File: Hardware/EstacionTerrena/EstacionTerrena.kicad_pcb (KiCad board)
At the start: 2 copper layers, 40 x 30 mm, 63 parts, among them J1 5-1814832-1, J2 USB_B_Micro, J3 ICSP, U1 TPD2E2U06, U2 MIC5353-3.3YMT, U3 PIC18F14K50, U4 CC1101RGP, U5 0915BM15A0001E, U6 B39921B3588U410, U7 CC1190, Y1 12MHz, Y2 26 MHz

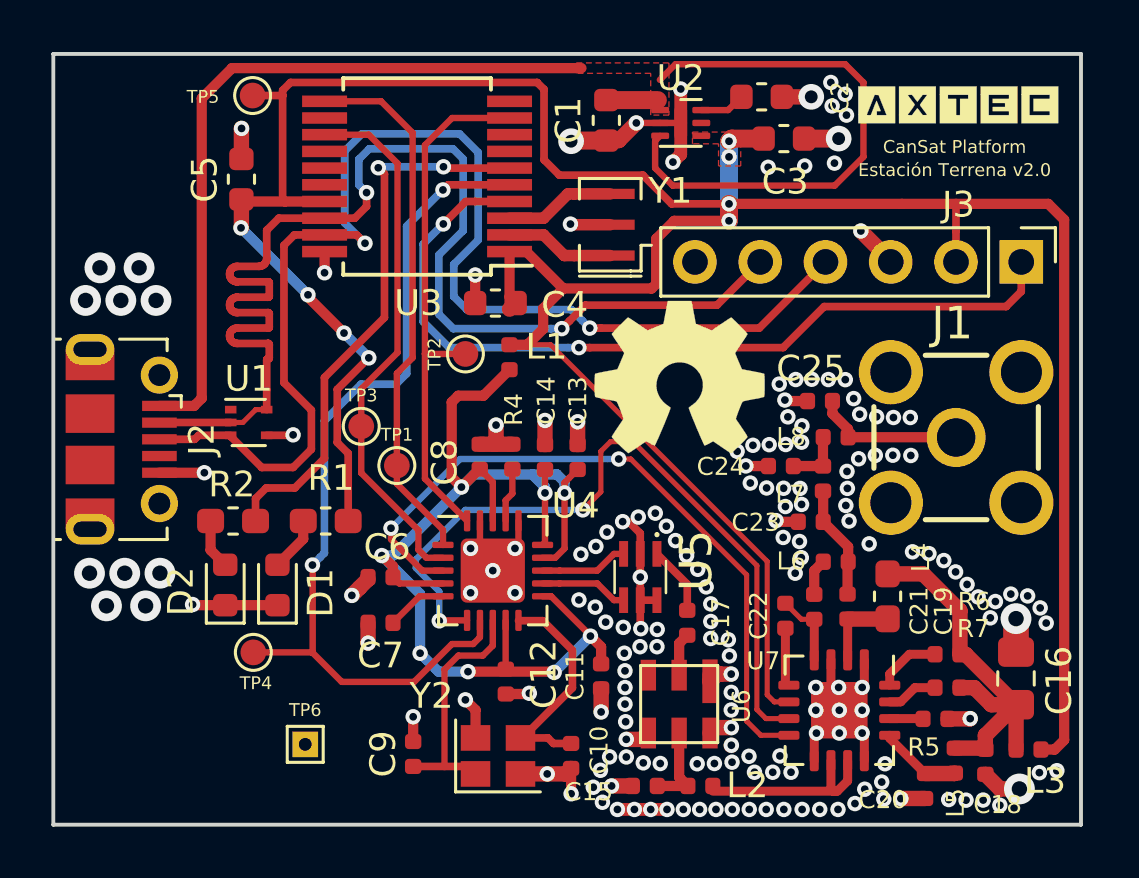
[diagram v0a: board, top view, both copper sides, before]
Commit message: Agregado jumper de selección de ganancia para CC1190 en ET
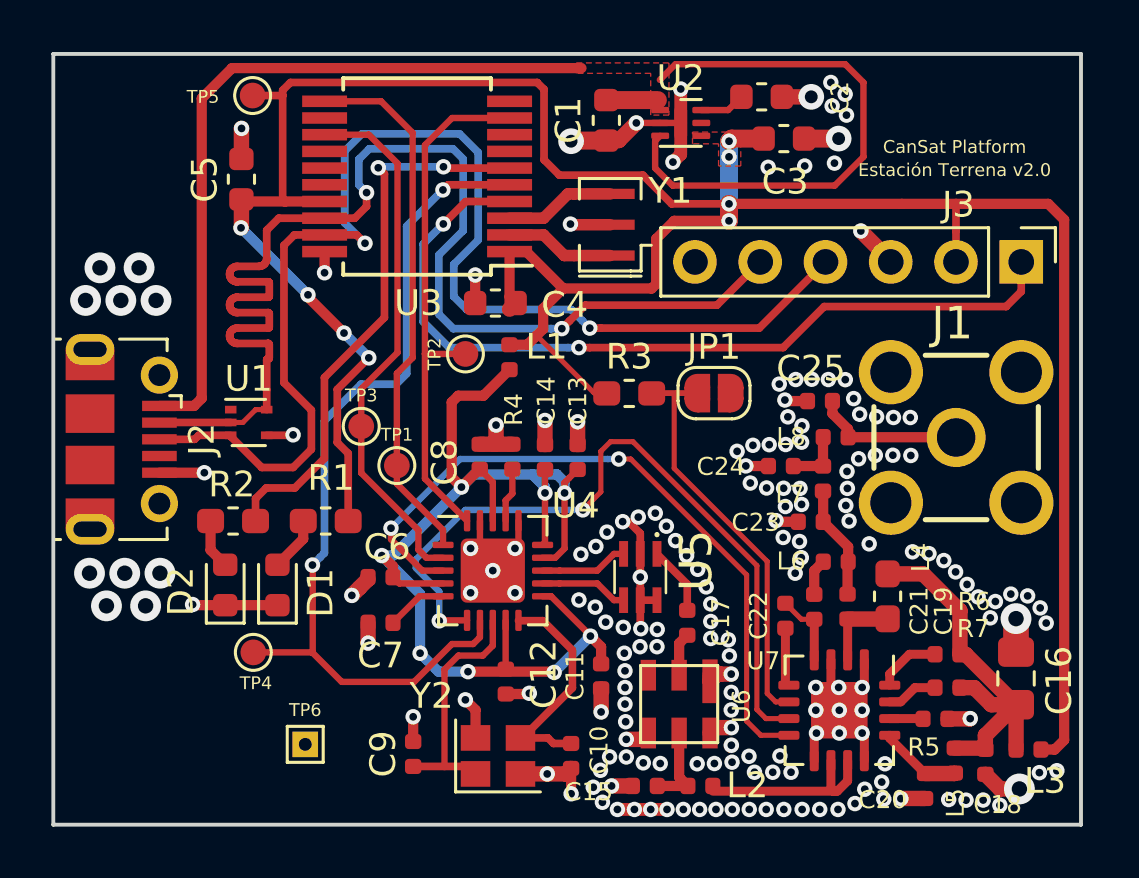
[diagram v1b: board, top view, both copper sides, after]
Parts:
- removed G*** (x2): LOGO, AXTEC:Logo_AXTEC
- removed REF** (x2): OSHW-Symbol_6.7x6mm_SilkScreen, Symbol:OSHW-Symbol_6.7x6mm_SilkScreen
- added JP1: Jumper, Jumper:SolderJumper-2_P1.3mm_Open_RoundedPad1.0x1.5mm, F.Cu at (25.7, 13.2)
- added R3: 10K, Resistor_SMD:R_0603_1608Metric_Pad1.05x0.95mm_HandSolder, F.Cu at (22.4, 13.2)
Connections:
- J2 pad 4: Net-(J2-Pad4) -> (no net)
- J3 pad 6: Net-(J3-Pad6) -> (no net)
- U1 pad 1: Net-(U1-Pad1) -> (no net)
- U2 pad 5: Net-(U2-Pad5) -> (no net)
- U3 pad 10: Net-(U3-Pad10) -> (no net)
- U3 pad 12: Net-(U3-Pad12) -> (no net)
- U3 pad 14: Net-(U3-Pad14) -> (no net)
- U3 pad 15: Net-(U3-Pad15) -> (no net)
- U3 pad 16: Net-(U3-Pad16) -> (no net)
- U3 pad 7: Net-(U3-Pad7) -> (no net)
- U3 pad 8: Net-(U3-Pad8) -> (no net)
- U7 pad 6: +3V3 -> /CC1101/HGM
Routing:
- net /CC1101/HGM: track 0.00 -> 17.6 mm
- net +3V3: track 125.2 -> 109.3 mm

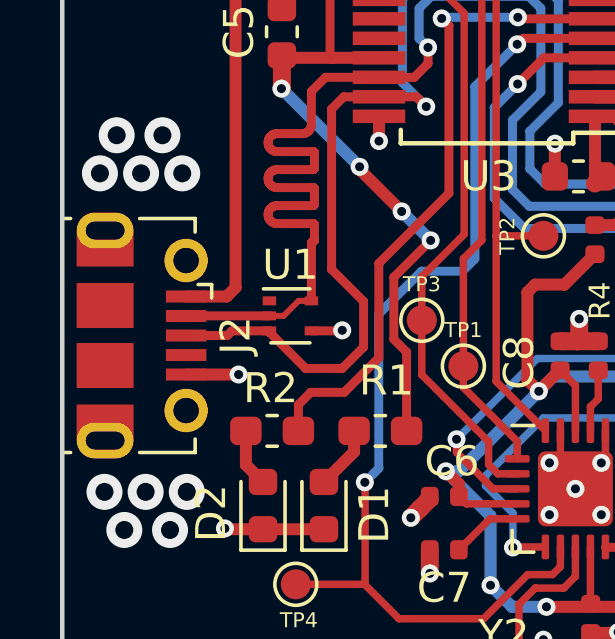
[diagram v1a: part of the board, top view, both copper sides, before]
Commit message: Nuevo conector USB para ET
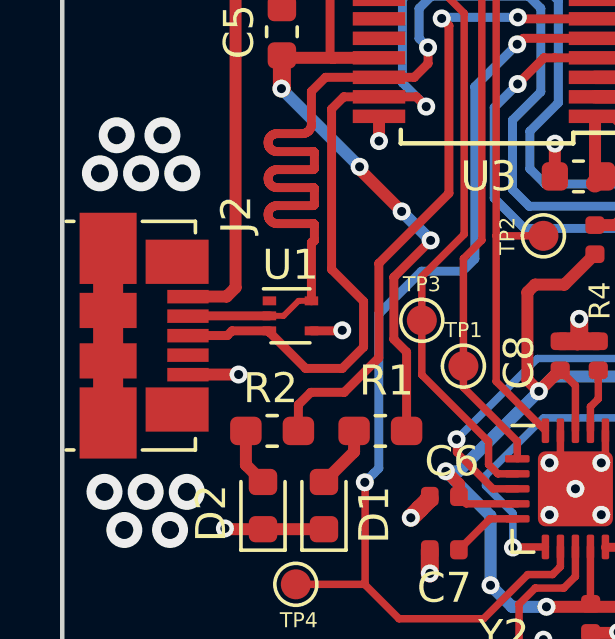
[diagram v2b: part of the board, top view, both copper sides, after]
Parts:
- J2: footprint Connector_USB:USB_Micro-B_Molex-105017-0001 -> Connector_USB:USB_Micro-B_Molex_47346-0001
- moved J2 0.06 mm to (2.73, 15.0)
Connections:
- J2 pad 4: (no net) -> Net-(J2-Pad4)
- J3 pad 6: (no net) -> Net-(J3-Pad6)
- U1 pad 1: (no net) -> Net-(U1-Pad1)
- U2 pad 5: (no net) -> Net-(U2-Pad5)
- U3 pad 10: (no net) -> Net-(U3-Pad10)
- U3 pad 12: (no net) -> Net-(U3-Pad12)
- U3 pad 14: (no net) -> Net-(U3-Pad14)
- U3 pad 15: (no net) -> Net-(U3-Pad15)
- U3 pad 16: (no net) -> Net-(U3-Pad16)
- U3 pad 7: (no net) -> Net-(U3-Pad7)
- U3 pad 8: (no net) -> Net-(U3-Pad8)
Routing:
- net GND: track 67.0 -> 72.8 mm

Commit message: Nuevos gerbers generados para todos los PCB
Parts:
- added G***: LOGO, AXTEC:Logo_AXTEC, B.Cu at (35.3, 1.77)
- added G***: LOGO, AXTEC:Logo_AXTEC, F.Cu at (35.4, 1.77)
- added REF**: OSHW-Symbol_6.7x6mm_SilkScreen, Symbol:OSHW-Symbol_6.7x6mm_SilkScreen, B.Cu at (4.15, 26.1)
- added REF**: OSHW-Symbol_6.7x6mm_SilkScreen, Symbol:OSHW-Symbol_6.7x6mm_SilkScreen, F.Cu at (4.15, 26.1)
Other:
- board text added: "ICSP"
